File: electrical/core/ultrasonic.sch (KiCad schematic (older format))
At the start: 7 parts, among them J8 Conn_01x04_Male, Q5 AO3400, Q6 AO3400

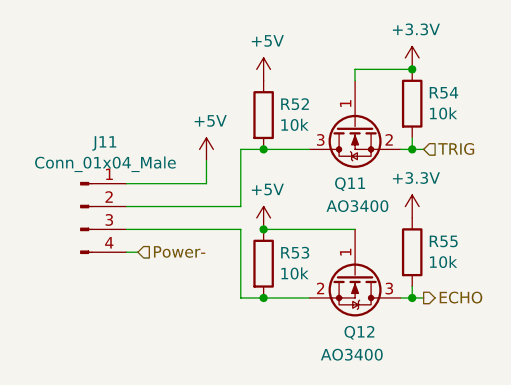
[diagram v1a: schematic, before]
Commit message: Changed RPi Buck to new model in order to support Jetson Nano boards
Fixed a bug in the Ultrassonic sensors level-shifters
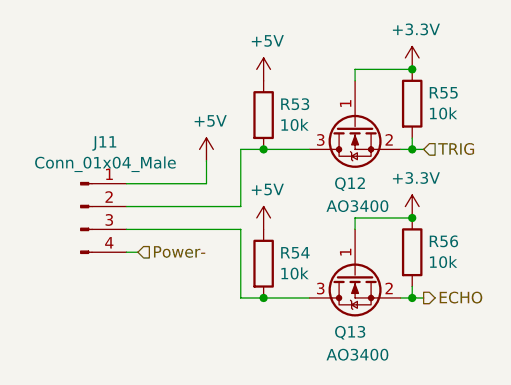
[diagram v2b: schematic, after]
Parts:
- renumbered Q5 to Q6, Q6 to Q7, R40 to R41, R41 to R42, R42 to R43, R43 to R44
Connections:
- net +3V3: now also Q7.1 (G)
- net +5V: no longer Q7.1 (G)
- net ECHO: now also Q7.2 (S); no longer Q7.3 (D)
- net at J8.3 (Pin_3), R42.2: now also Q7.3 (D); no longer Q7.2 (S)

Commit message: revert changes to Level-shifters. Optimize for single-direction operation
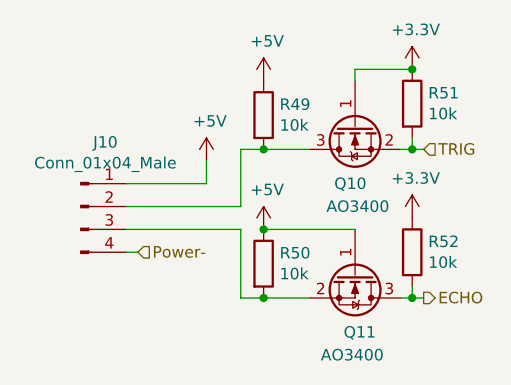
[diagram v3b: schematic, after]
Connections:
- net +3V3: no longer Q7.1 (G)
- net +5V: now also Q7.1 (G)
- net ECHO: now also Q7.3 (D); no longer Q7.2 (S)
- net at J8.3 (Pin_3), R42.2: now also Q7.2 (S); no longer Q7.3 (D)
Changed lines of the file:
@@
 AR Path="/5D1373A3/5E650C4B/5DB4719C" Ref="J10"  Part="1"
 AR Path="/5D1373A3/5E652B60/5DB4719C" Ref="J11"  Part="1"
-F 0 "J11" H 4758 4031 50  0000 C CNN
+F 0 "J10" H 4758 4031 50  0000 C CNN
 F 1 "Conn_01x04_Male" H 4758 3940 50  0000 C CNN
 F 2 "Connector_PinHeader_2.54mm:PinHeader_1x04_P2.54mm_Vertical" H 4650 3750 50  0001 C CNN
@@
 AR Path="/5D1373A3/5E650C4B/5DB471A5" Ref="#PWR0124"  Part="1"
 AR Path="/5D1373A3/5E652B60/5DB471A5" Ref="#PWR0129"  Part="1"
-F 0 "#PWR0129" H 5200 3400 50  0001 C CNN
+F 0 "#PWR0124" H 5200 3400 50  0001 C CNN
 F 1 "+5V" H 5215 3723 50  0000 C CNN
 F 2 "" H 5200 3550 50  0001 C CNN
@@
 AR Path="/5D1373A3/5E650C4B/5DB5AAB6" Ref="#PWR0125"  Part="1"
 AR Path="/5D1373A3/5E652B60/5DB5AAB6" Ref="#PWR0130"  Part="1"
-F 0 "#PWR0130" H 5450 3050 50  0001 C CNN
+F 0 "#PWR0125" H 5450 3050 50  0001 C CNN
 F 1 "+5V" H 5465 3373 50  0000 C CNN
 F 2 "" H 5450 3200 50  0001 C CNN
@@
 AR Path="/5D1373A3/5E650C4B/5DB62EEB" Ref="#PWR0127"  Part="1"
 AR Path="/5D1373A3/5E652B60/5DB62EEB" Ref="#PWR0132"  Part="1"
-F 0 "#PWR0132" H 6100 3000 50  0001 C CNN
+F 0 "#PWR0127" H 6100 3000 50  0001 C CNN
 F 1 "+3.3V" H 6115 3323 50  0000 C CNN
 F 2 "" H 6100 3150 50  0001 C CNN
@@
 AR Path="/5D1373A3/5E650C4B/5DB63B36" Ref="R50"  Part="1"
 AR Path="/5D1373A3/5E652B60/5DB63B36" Ref="R54"  Part="1"
-F 0 "R54" H 5520 4046 50  0000 L CNN
+F 0 "R50" H 5520 4046 50  0000 L CNN
 F 1 "10k" H 5520 3955 50  0000 L CNN
 F 2 "Resistor_SMD:R_0603_1608Metric" V 5380 4000 50  0001 C CNN
@@
 AR Path="/5D1373A3/5E650C4B/5DB640C0" Ref="R49"  Part="1"
 AR Path="/5D1373A3/5E652B60/5DB640C0" Ref="R53"  Part="1"
-F 0 "R53" H 5520 3396 50  0000 L CNN
+F 0 "R49" H 5520 3396 50  0000 L CNN
 F 1 "10k" H 5520 3305 50  0000 L CNN
 F 2 "Resistor_SMD:R_0603_1608Metric" V 5380 3350 50  0001 C CNN
@@
 AR Path="/5D1373A3/5E650C4B/5E635F70" Ref="Q10"  Part="1"
 AR Path="/5D1373A3/5E652B60/5E635F70" Ref="Q12"  Part="1"
-F 0 "Q12" V 6150 3300 50  0000 L CNN
+F 0 "Q10" V 6150 3300 50  0000 L CNN
 F 1 "AO3400" V 6250 3200 50  0000 L CNN
 F 2 "Package_TO_SOT_SMD:SOT-23" H 6675 3275 50  0001 C CNN
@@
 AR Path="/5D1373A3/5E650C4B/5E677DAA" Ref="Q11"  Part="1"
 AR Path="/5D1373A3/5E652B60/5E677DAA" Ref="Q13"  Part="1"
-F 0 "Q13" V 6150 3950 50  0000 L CNN
+F 0 "Q11" V 6150 3950 50  0000 L CNN
 F 1 "AO3400" V 6250 3850 50  0000 L CNN
 F 2 "Package_TO_SOT_SMD:SOT-23" H 6675 3925 50  0001 C CNN
 F 3 "http://www.aosmd.com/pdfs/datasheet/ao3400.pdf" H 5950 4000 50  0001 C CNN
 	1    5850 4000
-	0    -1   1    0
+	0    1    1    0
 $EndComp
 Wire Wire Line
@@
 AR Path="/5D1373A3/5E650C4B/5E680E9A" Ref="#PWR0126"  Part="1"
 AR Path="/5D1373A3/5E652B60/5E680E9A" Ref="#PWR0131"  Part="1"
-F 0 "#PWR0131" H 5450 3700 50  0001 C CNN
+F 0 "#PWR0126" H 5450 3700 50  0001 C CNN
 F 1 "+5V" H 5465 4023 50  0000 C CNN
 F 2 "" H 5450 3850 50  0001 C CNN
@@
 AR Path="/5D1373A3/5E650C4B/5E6822ED" Ref="R51"  Part="1"
 AR Path="/5D1373A3/5E652B60/5E6822ED" Ref="R55"  Part="1"
-F 0 "R55" H 6170 3346 50  0000 L CNN
+F 0 "R51" H 6170 3346 50  0000 L CNN
 F 1 "10k" H 6170 3255 50  0000 L CNN
 F 2 "Resistor_SMD:R_0603_1608Metric" V 6030 3300 50  0001 C CNN
@@
 AR Path="/5D1373A3/5E650C4B/5E6835CA" Ref="R52"  Part="1"
 AR Path="/5D1373A3/5E652B60/5E6835CA" Ref="R56"  Part="1"
-F 0 "R56" H 6170 3996 50  0000 L CNN
+F 0 "R52" H 6170 3996 50  0000 L CNN
 F 1 "10k" H 6170 3905 50  0000 L CNN
 F 2 "Resistor_SMD:R_0603_1608Metric" V 6030 3950 50  0001 C CNN
@@
 AR Path="/5D1373A3/5E650C4B/5E68391F" Ref="#PWR0128"  Part="1"
 AR Path="/5D1373A3/5E652B60/5E68391F" Ref="#PWR0133"  Part="1"
-F 0 "#PWR0133" H 6100 3650 50  0001 C CNN
+F 0 "#PWR0128" H 6100 3650 50  0001 C CNN
 F 1 "+3.3V" H 6115 3973 50  0000 C CNN
 F 2 "" H 6100 3800 50  0001 C CNN
@@
 Power-
 Wire Wire Line
-	5850 3850 5850 3800
-Wire Wire Line
-	5850 3800 6100 3800
-Connection ~ 6100 3800
+	5850 3850 5450 3850
+Connection ~ 5450 3850
 $EndSCHEMATC

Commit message: Review capacitors and warnings
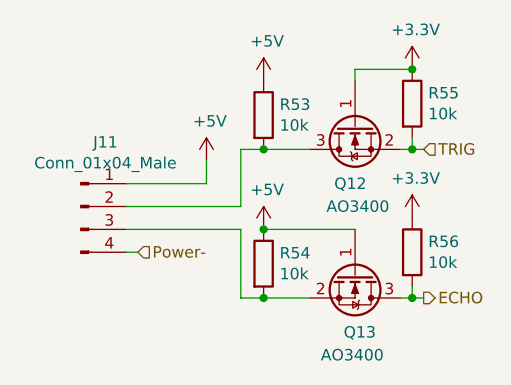
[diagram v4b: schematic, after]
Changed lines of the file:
@@
 AR Path="/5D1373A3/5E650C4B/5DB4719C" Ref="J10"  Part="1"
 AR Path="/5D1373A3/5E652B60/5DB4719C" Ref="J11"  Part="1"
-F 0 "J10" H 4758 4031 50  0000 C CNN
+F 0 "J11" H 4758 4031 50  0000 C CNN
 F 1 "Conn_01x04_Male" H 4758 3940 50  0000 C CNN
 F 2 "Connector_PinHeader_2.54mm:PinHeader_1x04_P2.54mm_Vertical" H 4650 3750 50  0001 C CNN
@@
 P 5200 3550
 AR Path="/5D1373A3/5DB471A5" Ref="#PWR?"  Part="1"
-AR Path="/5D1373A3/5DB42710/5DB471A5" Ref="#PWR0114"  Part="1"
+AR Path="/5D1373A3/5DB42710/5DB471A5" Ref="#PWR0116"  Part="1"
 AR Path="/5D1373A3/5DBA0DBB/5DB471A5" Ref="#PWR?"  Part="1"
 AR Path="/5D1373A3/5DBA1C1E/5DB471A5" Ref="#PWR?"  Part="1"
@@
 AR Path="/5D1373A3/5DBA7DAA/5DB471A5" Ref="#PWR?"  Part="1"
 AR Path="/5D1373A3/5DBA7DAF/5DB471A5" Ref="#PWR?"  Part="1"
-AR Path="/5D1373A3/5E6481EF/5DB471A5" Ref="#PWR0119"  Part="1"
-AR Path="/5D1373A3/5E650C4B/5DB471A5" Ref="#PWR0124"  Part="1"
-AR Path="/5D1373A3/5E652B60/5DB471A5" Ref="#PWR0129"  Part="1"
-F 0 "#PWR0124" H 5200 3400 50  0001 C CNN
+AR Path="/5D1373A3/5E6481EF/5DB471A5" Ref="#PWR0121"  Part="1"
+AR Path="/5D1373A3/5E650C4B/5DB471A5" Ref="#PWR0126"  Part="1"
+AR Path="/5D1373A3/5E652B60/5DB471A5" Ref="#PWR0131"  Part="1"
+F 0 "#PWR0131" H 5200 3400 50  0001 C CNN
 F 1 "+5V" H 5215 3723 50  0000 C CNN
 F 2 "" H 5200 3550 50  0001 C CNN
@@
 TRIG
 $Comp
-L power:+5V #PWR0115
+L power:+5V #PWR0117
 U 1 1 5DB5AAB6
 P 5450 3200
-AR Path="/5D1373A3/5DB42710/5DB5AAB6" Ref="#PWR0115"  Part="1"
+AR Path="/5D1373A3/5DB42710/5DB5AAB6" Ref="#PWR0117"  Part="1"
 AR Path="/5D1373A3/5DBA0DBB/5DB5AAB6" Ref="#PWR?"  Part="1"
 AR Path="/5D1373A3/5DBA1C1E/5DB5AAB6" Ref="#PWR?"  Part="1"
@@
 AR Path="/5D1373A3/5DBA7DAA/5DB5AAB6" Ref="#PWR?"  Part="1"
 AR Path="/5D1373A3/5DBA7DAF/5DB5AAB6" Ref="#PWR?"  Part="1"
-AR Path="/5D1373A3/5E6481EF/5DB5AAB6" Ref="#PWR0120"  Part="1"
-AR Path="/5D1373A3/5E650C4B/5DB5AAB6" Ref="#PWR0125"  Part="1"
-AR Path="/5D1373A3/5E652B60/5DB5AAB6" Ref="#PWR0130"  Part="1"
-F 0 "#PWR0125" H 5450 3050 50  0001 C CNN
+AR Path="/5D1373A3/5E6481EF/5DB5AAB6" Ref="#PWR0122"  Part="1"
+AR Path="/5D1373A3/5E650C4B/5DB5AAB6" Ref="#PWR0127"  Part="1"
+AR Path="/5D1373A3/5E652B60/5DB5AAB6" Ref="#PWR0132"  Part="1"
+F 0 "#PWR0132" H 5450 3050 50  0001 C CNN
 F 1 "+5V" H 5465 3373 50  0000 C CNN
 F 2 "" H 5450 3200 50  0001 C CNN
@@
 ECHO
 $Comp
-L power:+3.3V #PWR0117
+L power:+3.3V #PWR0119
 U 1 1 5DB62EEB
 P 6100 3150
-AR Path="/5D1373A3/5DB42710/5DB62EEB" Ref="#PWR0117"  Part="1"
+AR Path="/5D1373A3/5DB42710/5DB62EEB" Ref="#PWR0119"  Part="1"
 AR Path="/5D1373A3/5DBA0DBB/5DB62EEB" Ref="#PWR?"  Part="1"
 AR Path="/5D1373A3/5DBA1C1E/5DB62EEB" Ref="#PWR?"  Part="1"
@@
 AR Path="/5D1373A3/5DBA7DAA/5DB62EEB" Ref="#PWR?"  Part="1"
 AR Path="/5D1373A3/5DBA7DAF/5DB62EEB" Ref="#PWR?"  Part="1"
-AR Path="/5D1373A3/5E6481EF/5DB62EEB" Ref="#PWR0122"  Part="1"
-AR Path="/5D1373A3/5E650C4B/5DB62EEB" Ref="#PWR0127"  Part="1"
-AR Path="/5D1373A3/5E652B60/5DB62EEB" Ref="#PWR0132"  Part="1"
-F 0 "#PWR0127" H 6100 3000 50  0001 C CNN
+AR Path="/5D1373A3/5E6481EF/5DB62EEB" Ref="#PWR0124"  Part="1"
+AR Path="/5D1373A3/5E650C4B/5DB62EEB" Ref="#PWR0129"  Part="1"
+AR Path="/5D1373A3/5E652B60/5DB62EEB" Ref="#PWR0134"  Part="1"
+F 0 "#PWR0134" H 6100 3000 50  0001 C CNN
 F 1 "+3.3V" H 6115 3323 50  0000 C CNN
 F 2 "" H 6100 3150 50  0001 C CNN
@@
 AR Path="/5D1373A3/5E650C4B/5DB63B36" Ref="R50"  Part="1"
 AR Path="/5D1373A3/5E652B60/5DB63B36" Ref="R54"  Part="1"
-F 0 "R50" H 5520 4046 50  0000 L CNN
+F 0 "R54" H 5520 4046 50  0000 L CNN
 F 1 "10k" H 5520 3955 50  0000 L CNN
 F 2 "Resistor_SMD:R_0603_1608Metric" V 5380 4000 50  0001 C CNN
@@
 AR Path="/5D1373A3/5E650C4B/5DB640C0" Ref="R49"  Part="1"
 AR Path="/5D1373A3/5E652B60/5DB640C0" Ref="R53"  Part="1"
-F 0 "R49" H 5520 3396 50  0000 L CNN
+F 0 "R53" H 5520 3396 50  0000 L CNN
 F 1 "10k" H 5520 3305 50  0000 L CNN
 F 2 "Resistor_SMD:R_0603_1608Metric" V 5380 3350 50  0001 C CNN
@@
 AR Path="/5D1373A3/5E650C4B/5E635F70" Ref="Q10"  Part="1"
 AR Path="/5D1373A3/5E652B60/5E635F70" Ref="Q12"  Part="1"
-F 0 "Q10" V 6150 3300 50  0000 L CNN
+F 0 "Q12" V 6150 3300 50  0000 L CNN
 F 1 "AO3400" V 6250 3200 50  0000 L CNN
 F 2 "Package_TO_SOT_SMD:SOT-23" H 6675 3275 50  0001 C CNN
@@
 AR Path="/5D1373A3/5E650C4B/5E677DAA" Ref="Q11"  Part="1"
 AR Path="/5D1373A3/5E652B60/5E677DAA" Ref="Q13"  Part="1"
-F 0 "Q11" V 6150 3950 50  0000 L CNN
+F 0 "Q13" V 6150 3950 50  0000 L CNN
 F 1 "AO3400" V 6250 3850 50  0000 L CNN
 F 2 "Package_TO_SOT_SMD:SOT-23" H 6675 3925 50  0001 C CNN
@@
 	5450 3500 5650 3500
 $Comp
-L power:+5V #PWR0116
+L power:+5V #PWR0118
 U 1 1 5E680E9A
 P 5450 3850
-AR Path="/5D1373A3/5DB42710/5E680E9A" Ref="#PWR0116"  Part="1"
+AR Path="/5D1373A3/5DB42710/5E680E9A" Ref="#PWR0118"  Part="1"
 AR Path="/5D1373A3/5DBA0DBB/5E680E9A" Ref="#PWR?"  Part="1"
 AR Path="/5D1373A3/5DBA1C1E/5E680E9A" Ref="#PWR?"  Part="1"
@@
 AR Path="/5D1373A3/5DBA7DAA/5E680E9A" Ref="#PWR?"  Part="1"
 AR Path="/5D1373A3/5DBA7DAF/5E680E9A" Ref="#PWR?"  Part="1"
-AR Path="/5D1373A3/5E6481EF/5E680E9A" Ref="#PWR0121"  Part="1"
-AR Path="/5D1373A3/5E650C4B/5E680E9A" Ref="#PWR0126"  Part="1"
-AR Path="/5D1373A3/5E652B60/5E680E9A" Ref="#PWR0131"  Part="1"
-F 0 "#PWR0126" H 5450 3700 50  0001 C CNN
+AR Path="/5D1373A3/5E6481EF/5E680E9A" Ref="#PWR0123"  Part="1"
+AR Path="/5D1373A3/5E650C4B/5E680E9A" Ref="#PWR0128"  Part="1"
+AR Path="/5D1373A3/5E652B60/5E680E9A" Ref="#PWR0133"  Part="1"
+F 0 "#PWR0133" H 5450 3700 50  0001 C CNN
 F 1 "+5V" H 5465 4023 50  0000 C CNN
 F 2 "" H 5450 3850 50  0001 C CNN
@@
 AR Path="/5D1373A3/5E650C4B/5E6822ED" Ref="R51"  Part="1"
 AR Path="/5D1373A3/5E652B60/5E6822ED" Ref="R55"  Part="1"
-F 0 "R51" H 6170 3346 50  0000 L CNN
+F 0 "R55" H 6170 3346 50  0000 L CNN
 F 1 "10k" H 6170 3255 50  0000 L CNN
 F 2 "Resistor_SMD:R_0603_1608Metric" V 6030 3300 50  0001 C CNN
@@
 AR Path="/5D1373A3/5E650C4B/5E6835CA" Ref="R52"  Part="1"
 AR Path="/5D1373A3/5E652B60/5E6835CA" Ref="R56"  Part="1"
-F 0 "R52" H 6170 3996 50  0000 L CNN
+F 0 "R56" H 6170 3996 50  0000 L CNN
 F 1 "10k" H 6170 3905 50  0000 L CNN
 F 2 "Resistor_SMD:R_0603_1608Metric" V 6030 3950 50  0001 C CNN
@@
 $EndComp
 $Comp
-L power:+3.3V #PWR0118
+L power:+3.3V #PWR0120
 U 1 1 5E68391F
 P 6100 3800
-AR Path="/5D1373A3/5DB42710/5E68391F" Ref="#PWR0118"  Part="1"
+AR Path="/5D1373A3/5DB42710/5E68391F" Ref="#PWR0120"  Part="1"
 AR Path="/5D1373A3/5DBA0DBB/5E68391F" Ref="#PWR?"  Part="1"
 AR Path="/5D1373A3/5DBA1C1E/5E68391F" Ref="#PWR?"  Part="1"
@@
 AR Path="/5D1373A3/5DBA7DAA/5E68391F" Ref="#PWR?"  Part="1"
 AR Path="/5D1373A3/5DBA7DAF/5E68391F" Ref="#PWR?"  Part="1"
-AR Path="/5D1373A3/5E6481EF/5E68391F" Ref="#PWR0123"  Part="1"
-AR Path="/5D1373A3/5E650C4B/5E68391F" Ref="#PWR0128"  Part="1"
-AR Path="/5D1373A3/5E652B60/5E68391F" Ref="#PWR0133"  Part="1"
-F 0 "#PWR0128" H 6100 3650 50  0001 C CNN
+AR Path="/5D1373A3/5E6481EF/5E68391F" Ref="#PWR0125"  Part="1"
+AR Path="/5D1373A3/5E650C4B/5E68391F" Ref="#PWR0130"  Part="1"
+AR Path="/5D1373A3/5E652B60/5E68391F" Ref="#PWR0135"  Part="1"
+F 0 "#PWR0135" H 6100 3650 50  0001 C CNN
 F 1 "+3.3V" H 6115 3973 50  0000 C CNN
 F 2 "" H 6100 3800 50  0001 C CNN

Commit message: Reannotated Schematics
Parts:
- renumbered R41 to R40, R42 to R41, R43 to R42, R44 to R43
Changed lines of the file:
@@
 P 5200 3550
 AR Path="/5D1373A3/5DB471A5" Ref="#PWR?"  Part="1"
-AR Path="/5D1373A3/5DB42710/5DB471A5" Ref="#PWR0116"  Part="1"
+AR Path="/5D1373A3/5DB42710/5DB471A5" Ref="#PWR0114"  Part="1"
 AR Path="/5D1373A3/5DBA0DBB/5DB471A5" Ref="#PWR?"  Part="1"
 AR Path="/5D1373A3/5DBA1C1E/5DB471A5" Ref="#PWR?"  Part="1"
@@
 AR Path="/5D1373A3/5DBA7DAA/5DB471A5" Ref="#PWR?"  Part="1"
 AR Path="/5D1373A3/5DBA7DAF/5DB471A5" Ref="#PWR?"  Part="1"
-AR Path="/5D1373A3/5E6481EF/5DB471A5" Ref="#PWR0121"  Part="1"
-AR Path="/5D1373A3/5E650C4B/5DB471A5" Ref="#PWR0126"  Part="1"
-AR Path="/5D1373A3/5E652B60/5DB471A5" Ref="#PWR0131"  Part="1"
-F 0 "#PWR0131" H 5200 3400 50  0001 C CNN
+AR Path="/5D1373A3/5E6481EF/5DB471A5" Ref="#PWR0119"  Part="1"
+AR Path="/5D1373A3/5E650C4B/5DB471A5" Ref="#PWR0124"  Part="1"
+AR Path="/5D1373A3/5E652B60/5DB471A5" Ref="#PWR0129"  Part="1"
+F 0 "#PWR0129" H 5200 3400 50  0001 C CNN
 F 1 "+5V" H 5215 3723 50  0000 C CNN
 F 2 "" H 5200 3550 50  0001 C CNN
@@
 TRIG
 $Comp
-L power:+5V #PWR0117
+L power:+5V #PWR0115
 U 1 1 5DB5AAB6
 P 5450 3200
-AR Path="/5D1373A3/5DB42710/5DB5AAB6" Ref="#PWR0117"  Part="1"
+AR Path="/5D1373A3/5DB42710/5DB5AAB6" Ref="#PWR0115"  Part="1"
 AR Path="/5D1373A3/5DBA0DBB/5DB5AAB6" Ref="#PWR?"  Part="1"
 AR Path="/5D1373A3/5DBA1C1E/5DB5AAB6" Ref="#PWR?"  Part="1"
@@
 AR Path="/5D1373A3/5DBA7DAA/5DB5AAB6" Ref="#PWR?"  Part="1"
 AR Path="/5D1373A3/5DBA7DAF/5DB5AAB6" Ref="#PWR?"  Part="1"
-AR Path="/5D1373A3/5E6481EF/5DB5AAB6" Ref="#PWR0122"  Part="1"
-AR Path="/5D1373A3/5E650C4B/5DB5AAB6" Ref="#PWR0127"  Part="1"
-AR Path="/5D1373A3/5E652B60/5DB5AAB6" Ref="#PWR0132"  Part="1"
-F 0 "#PWR0132" H 5450 3050 50  0001 C CNN
+AR Path="/5D1373A3/5E6481EF/5DB5AAB6" Ref="#PWR0120"  Part="1"
+AR Path="/5D1373A3/5E650C4B/5DB5AAB6" Ref="#PWR0125"  Part="1"
+AR Path="/5D1373A3/5E652B60/5DB5AAB6" Ref="#PWR0130"  Part="1"
+F 0 "#PWR0130" H 5450 3050 50  0001 C CNN
 F 1 "+5V" H 5465 3373 50  0000 C CNN
 F 2 "" H 5450 3200 50  0001 C CNN
@@
 ECHO
 $Comp
-L power:+3.3V #PWR0119
+L power:+3.3V #PWR0117
 U 1 1 5DB62EEB
 P 6100 3150
-AR Path="/5D1373A3/5DB42710/5DB62EEB" Ref="#PWR0119"  Part="1"
+AR Path="/5D1373A3/5DB42710/5DB62EEB" Ref="#PWR0117"  Part="1"
 AR Path="/5D1373A3/5DBA0DBB/5DB62EEB" Ref="#PWR?"  Part="1"
 AR Path="/5D1373A3/5DBA1C1E/5DB62EEB" Ref="#PWR?"  Part="1"
@@
 AR Path="/5D1373A3/5DBA7DAA/5DB62EEB" Ref="#PWR?"  Part="1"
 AR Path="/5D1373A3/5DBA7DAF/5DB62EEB" Ref="#PWR?"  Part="1"
-AR Path="/5D1373A3/5E6481EF/5DB62EEB" Ref="#PWR0124"  Part="1"
-AR Path="/5D1373A3/5E650C4B/5DB62EEB" Ref="#PWR0129"  Part="1"
-AR Path="/5D1373A3/5E652B60/5DB62EEB" Ref="#PWR0134"  Part="1"
-F 0 "#PWR0134" H 6100 3000 50  0001 C CNN
+AR Path="/5D1373A3/5E6481EF/5DB62EEB" Ref="#PWR0122"  Part="1"
+AR Path="/5D1373A3/5E650C4B/5DB62EEB" Ref="#PWR0127"  Part="1"
+AR Path="/5D1373A3/5E652B60/5DB62EEB" Ref="#PWR0132"  Part="1"
+F 0 "#PWR0132" H 6100 3000 50  0001 C CNN
 F 1 "+3.3V" H 6115 3323 50  0000 C CNN
 F 2 "" H 6100 3150 50  0001 C CNN
@@
 $EndComp
 $Comp
-L Device:R R42
+L Device:R R41
 U 1 1 5DB63B36
 P 5450 4000
-AR Path="/5D1373A3/5DB42710/5DB63B36" Ref="R42"  Part="1"
+AR Path="/5D1373A3/5DB42710/5DB63B36" Ref="R41"  Part="1"
 AR Path="/5D1373A3/5DBA0DBB/5DB63B36" Ref="R?"  Part="1"
 AR Path="/5D1373A3/5DBA1C1E/5DB63B36" Ref="R?"  Part="1"
@@
 AR Path="/5D1373A3/5DBA7DAA/5DB63B36" Ref="R?"  Part="1"
 AR Path="/5D1373A3/5DBA7DAF/5DB63B36" Ref="R?"  Part="1"
-AR Path="/5D1373A3/5E6481EF/5DB63B36" Ref="R46"  Part="1"
-AR Path="/5D1373A3/5E650C4B/5DB63B36" Ref="R50"  Part="1"
-AR Path="/5D1373A3/5E652B60/5DB63B36" Ref="R54"  Part="1"
-F 0 "R54" H 5520 4046 50  0000 L CNN
+AR Path="/5D1373A3/5E6481EF/5DB63B36" Ref="R45"  Part="1"
+AR Path="/5D1373A3/5E650C4B/5DB63B36" Ref="R49"  Part="1"
+AR Path="/5D1373A3/5E652B60/5DB63B36" Ref="R53"  Part="1"
+F 0 "R53" H 5520 4046 50  0000 L CNN
 F 1 "10k" H 5520 3955 50  0000 L CNN
 F 2 "Resistor_SMD:R_0603_1608Metric" V 5380 4000 50  0001 C CNN
@@
 $EndComp
 $Comp
-L Device:R R41
+L Device:R R40
 U 1 1 5DB640C0
 P 5450 3350
-AR Path="/5D1373A3/5DB42710/5DB640C0" Ref="R41"  Part="1"
+AR Path="/5D1373A3/5DB42710/5DB640C0" Ref="R40"  Part="1"
 AR Path="/5D1373A3/5DBA0DBB/5DB640C0" Ref="R?"  Part="1"
 AR Path="/5D1373A3/5DBA1C1E/5DB640C0" Ref="R?"  Part="1"
@@
 AR Path="/5D1373A3/5DBA7DAA/5DB640C0" Ref="R?"  Part="1"
 AR Path="/5D1373A3/5DBA7DAF/5DB640C0" Ref="R?"  Part="1"
-AR Path="/5D1373A3/5E6481EF/5DB640C0" Ref="R45"  Part="1"
-AR Path="/5D1373A3/5E650C4B/5DB640C0" Ref="R49"  Part="1"
-AR Path="/5D1373A3/5E652B60/5DB640C0" Ref="R53"  Part="1"
-F 0 "R53" H 5520 3396 50  0000 L CNN
+AR Path="/5D1373A3/5E6481EF/5DB640C0" Ref="R44"  Part="1"
+AR Path="/5D1373A3/5E650C4B/5DB640C0" Ref="R48"  Part="1"
+AR Path="/5D1373A3/5E652B60/5DB640C0" Ref="R52"  Part="1"
+F 0 "R52" H 5520 3396 50  0000 L CNN
 F 1 "10k" H 5520 3305 50  0000 L CNN
 F 2 "Resistor_SMD:R_0603_1608Metric" V 5380 3350 50  0001 C CNN
@@
 	5450 3500 5650 3500
 $Comp
-L power:+5V #PWR0118
+L power:+5V #PWR0116
 U 1 1 5E680E9A
 P 5450 3850
-AR Path="/5D1373A3/5DB42710/5E680E9A" Ref="#PWR0118"  Part="1"
+AR Path="/5D1373A3/5DB42710/5E680E9A" Ref="#PWR0116"  Part="1"
 AR Path="/5D1373A3/5DBA0DBB/5E680E9A" Ref="#PWR?"  Part="1"
 AR Path="/5D1373A3/5DBA1C1E/5E680E9A" Ref="#PWR?"  Part="1"
@@
 AR Path="/5D1373A3/5DBA7DAA/5E680E9A" Ref="#PWR?"  Part="1"
 AR Path="/5D1373A3/5DBA7DAF/5E680E9A" Ref="#PWR?"  Part="1"
-AR Path="/5D1373A3/5E6481EF/5E680E9A" Ref="#PWR0123"  Part="1"
-AR Path="/5D1373A3/5E650C4B/5E680E9A" Ref="#PWR0128"  Part="1"
-AR Path="/5D1373A3/5E652B60/5E680E9A" Ref="#PWR0133"  Part="1"
-F 0 "#PWR0133" H 5450 3700 50  0001 C CNN
+AR Path="/5D1373A3/5E6481EF/5E680E9A" Ref="#PWR0121"  Part="1"
+AR Path="/5D1373A3/5E650C4B/5E680E9A" Ref="#PWR0126"  Part="1"
+AR Path="/5D1373A3/5E652B60/5E680E9A" Ref="#PWR0131"  Part="1"
+F 0 "#PWR0131" H 5450 3700 50  0001 C CNN
 F 1 "+5V" H 5465 4023 50  0000 C CNN
 F 2 "" H 5450 3850 50  0001 C CNN
@@
 	5450 4150 5350 4150
 $Comp
-L Device:R R43
+L Device:R R42
 U 1 1 5E6822ED
 P 6100 3300
-AR Path="/5D1373A3/5DB42710/5E6822ED" Ref="R43"  Part="1"
+AR Path="/5D1373A3/5DB42710/5E6822ED" Ref="R42"  Part="1"
 AR Path="/5D1373A3/5DBA0DBB/5E6822ED" Ref="R?"  Part="1"
 AR Path="/5D1373A3/5DBA1C1E/5E6822ED" Ref="R?"  Part="1"
@@
 AR Path="/5D1373A3/5DBA7DAA/5E6822ED" Ref="R?"  Part="1"
 AR Path="/5D1373A3/5DBA7DAF/5E6822ED" Ref="R?"  Part="1"
-AR Path="/5D1373A3/5E6481EF/5E6822ED" Ref="R47"  Part="1"
-AR Path="/5D1373A3/5E650C4B/5E6822ED" Ref="R51"  Part="1"
-AR Path="/5D1373A3/5E652B60/5E6822ED" Ref="R55"  Part="1"
-F 0 "R55" H 6170 3346 50  0000 L CNN
+AR Path="/5D1373A3/5E6481EF/5E6822ED" Ref="R46"  Part="1"
+AR Path="/5D1373A3/5E650C4B/5E6822ED" Ref="R50"  Part="1"
+AR Path="/5D1373A3/5E652B60/5E6822ED" Ref="R54"  Part="1"
+F 0 "R54" H 6170 3346 50  0000 L CNN
 F 1 "10k" H 6170 3255 50  0000 L CNN
 F 2 "Resistor_SMD:R_0603_1608Metric" V 6030 3300 50  0001 C CNN
@@
 Connection ~ 6100 3500
 $Comp
-L Device:R R44
+L Device:R R43
 U 1 1 5E6835CA
 P 6100 3950
-AR Path="/5D1373A3/5DB42710/5E6835CA" Ref="R44"  Part="1"
+AR Path="/5D1373A3/5DB42710/5E6835CA" Ref="R43"  Part="1"
 AR Path="/5D1373A3/5DBA0DBB/5E6835CA" Ref="R?"  Part="1"
 AR Path="/5D1373A3/5DBA1C1E/5E6835CA" Ref="R?"  Part="1"
@@
 AR Path="/5D1373A3/5DBA7DAA/5E6835CA" Ref="R?"  Part="1"
 AR Path="/5D1373A3/5DBA7DAF/5E6835CA" Ref="R?"  Part="1"
-AR Path="/5D1373A3/5E6481EF/5E6835CA" Ref="R48"  Part="1"
-AR Path="/5D1373A3/5E650C4B/5E6835CA" Ref="R52"  Part="1"
-AR Path="/5D1373A3/5E652B60/5E6835CA" Ref="R56"  Part="1"
-F 0 "R56" H 6170 3996 50  0000 L CNN
+AR Path="/5D1373A3/5E6481EF/5E6835CA" Ref="R47"  Part="1"
+AR Path="/5D1373A3/5E650C4B/5E6835CA" Ref="R51"  Part="1"
+AR Path="/5D1373A3/5E652B60/5E6835CA" Ref="R55"  Part="1"
+F 0 "R55" H 6170 3996 50  0000 L CNN
 F 1 "10k" H 6170 3905 50  0000 L CNN
 F 2 "Resistor_SMD:R_0603_1608Metric" V 6030 3950 50  0001 C CNN
@@
 $EndComp
 $Comp
-L power:+3.3V #PWR0120
+L power:+3.3V #PWR0118
 U 1 1 5E68391F
 P 6100 3800
-AR Path="/5D1373A3/5DB42710/5E68391F" Ref="#PWR0120"  Part="1"
+AR Path="/5D1373A3/5DB42710/5E68391F" Ref="#PWR0118"  Part="1"
 AR Path="/5D1373A3/5DBA0DBB/5E68391F" Ref="#PWR?"  Part="1"
 AR Path="/5D1373A3/5DBA1C1E/5E68391F" Ref="#PWR?"  Part="1"
@@
 AR Path="/5D1373A3/5DBA7DAA/5E68391F" Ref="#PWR?"  Part="1"
 AR Path="/5D1373A3/5DBA7DAF/5E68391F" Ref="#PWR?"  Part="1"
-AR Path="/5D1373A3/5E6481EF/5E68391F" Ref="#PWR0125"  Part="1"
-AR Path="/5D1373A3/5E650C4B/5E68391F" Ref="#PWR0130"  Part="1"
-AR Path="/5D1373A3/5E652B60/5E68391F" Ref="#PWR0135"  Part="1"
-F 0 "#PWR0135" H 6100 3650 50  0001 C CNN
+AR Path="/5D1373A3/5E6481EF/5E68391F" Ref="#PWR0123"  Part="1"
+AR Path="/5D1373A3/5E650C4B/5E68391F" Ref="#PWR0128"  Part="1"
+AR Path="/5D1373A3/5E652B60/5E68391F" Ref="#PWR0133"  Part="1"
+F 0 "#PWR0133" H 6100 3650 50  0001 C CNN
 F 1 "+3.3V" H 6115 3973 50  0000 C CNN
 F 2 "" H 6100 3800 50  0001 C CNN

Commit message: connections
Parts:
- renumbered J8 to J4, Q6 to Q5, Q7 to Q6, R40 to R27, R41 to R28, R42 to R29, R43 to R30
